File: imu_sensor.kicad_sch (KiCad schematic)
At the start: 10 parts, among them J2 JST_PH2.0_01x04, U1 LSM6DSL, U2 LIS2MDL

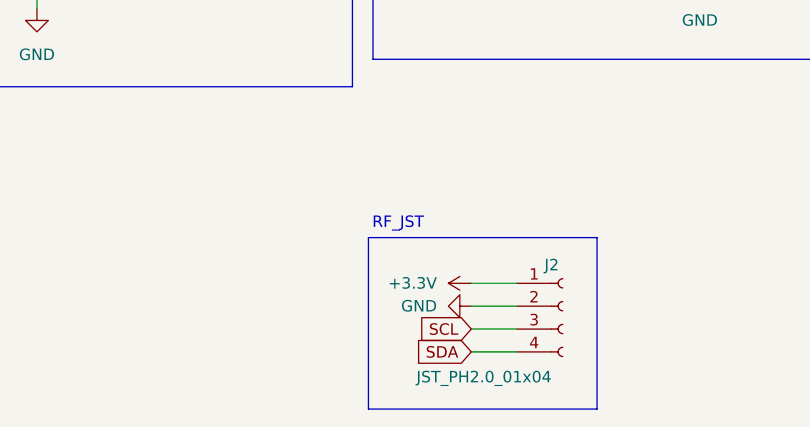
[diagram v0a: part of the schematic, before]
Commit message: Route Traces for ESP32 and related IO
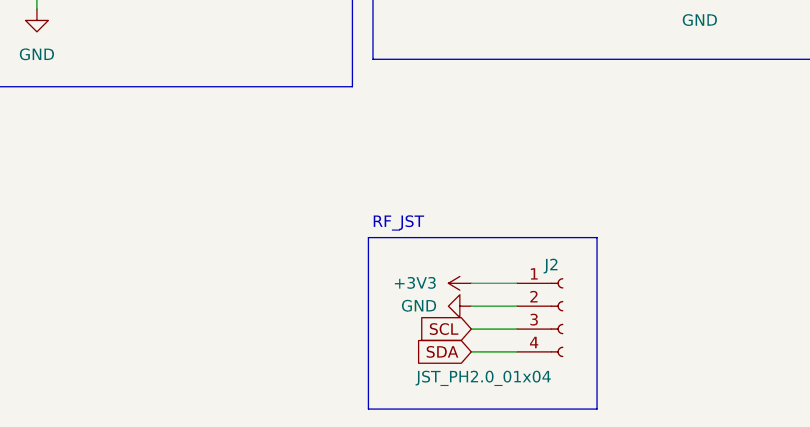
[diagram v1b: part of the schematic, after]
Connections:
- net +3.3V is gone; now on net +3V3: J2.1 (Pin_1)
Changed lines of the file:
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@@
 			)
 		)
-		(property "Value" "+3.3V"
+		(property "Value" "+3V3"
 			(at 118.11 121.9199 90)
 			(effects

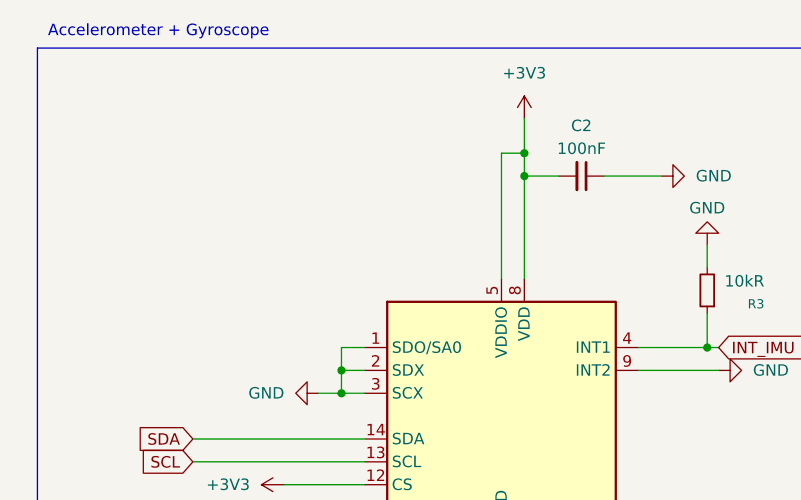
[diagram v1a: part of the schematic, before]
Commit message: Add Sensors and Silkscreen Adjustments
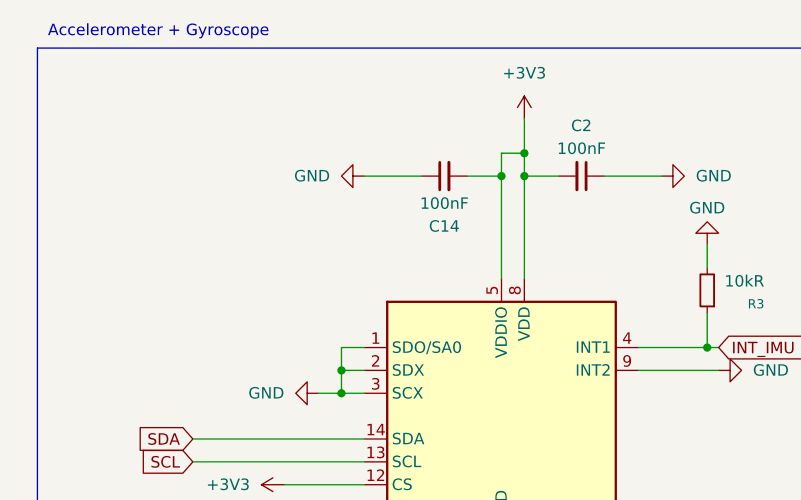
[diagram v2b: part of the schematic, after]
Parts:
- added C14: 100nF, Capacitor_SMD:C_0805_2012Metric_Pad1.18x1.45mm_HandSolder, symbol Device:C_Small
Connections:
- net +3V3: now also C14.2
- net GND: now also C14.1
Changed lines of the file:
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@@
+	)
+	(junction
+		(at 73.66 40.64)
+		(diameter 0)
+		(color 0 0 0 0)
 	)
 	(junction
@@
 	(wire
 		(pts
+			(xy 64.77 40.64) (xy 58.42 40.64)
+		)
+		(stroke
+			(width 0)
+			(type default)
+		)
+	)
+	(wire
+		(pts
 			(xy 172.72 59.69) (xy 172.72 62.23)
 		)
@@
 	(wire
 		(pts
+			(xy 69.85 40.64) (xy 73.66 40.64)
+		)
+		(stroke
+			(width 0)
+			(type default)
+		)
+	)
+	(wire
+		(pts
 			(xy 119.38 64.77) (xy 134.62 64.77)
 		)
@@
 	(wire
 		(pts
-			(xy 73.66 38.1) (xy 73.66 52.07)
+			(xy 73.66 38.1) (xy 73.66 40.64)
 		)
 		(stroke
@@
 		(pts
 			(xy 147.32 35.56) (xy 147.32 38.1)
+		)
+		(stroke
+			(width 0)
+			(type default)
+		)
+	)
+	(wire
+		(pts
+			(xy 73.66 40.64) (xy 73.66 52.07)
 		)
 		(stroke
@@
 	)
 	(symbol
+		(lib_id "Device:C_Small")
+		(at 67.31 40.64 90)
+		(mirror x)
+		(unit 1)
+		(exclude_from_sim no)
+		(in_bom yes)
+		(on_board yes)
+		(dnp no)
+		(property "Reference" "C14"
+			(at 67.31 46.228 90)
+			(effects
+				(font
+					(size 1.27 1.27)
+				)
+			)
+		)
+		(property "Value" "100nF"
+			(at 67.31 43.688 90)
+			(effects
+				(font
+					(size 1.27 1.27)
+				)
+			)
+		)
+		(property "Footprint" "Capacitor_SMD:C_0805_2012Metric_Pad1.18x1.45mm_HandSolder"
+			(at 67.31 40.64 0)
+			(effects
+				(font
+					(size 1.27 1.27)
+				)
+				(hide yes)
+			)
+		)
+		(property "Datasheet" "~"
+			(at 67.31 40.64 0)
+			(effects
+				(font
+					(size 1.27 1.27)
+				)
+				(hide yes)
+			)
+		)
+		(property "Description" "Unpolarized capacitor, small symbol"
+			(at 67.31 40.64 0)
+			(effects
+				(font
+					(size 1.27 1.27)
+				)
+				(hide yes)
+			)
+		)
+		(pin "2"
+		)
+		(pin "1"
+		)
+		(instances
+			(project "imu"
+				(path "/c0c3b276-ae23-48c2-9824-bf30dce5574d/819dc26d-f273-4edf-ac8c-4ee164d27f8f"
+					(reference "C14")
+					(unit 1)
+				)
+			)
+		)
+	)
+	(symbol
 		(lib_id "power:GND")
 		(at 53.34 64.77 270)
@@
 					(unit 1)
 				)
+			)
+		)
+	)
+	(symbol
+		(lib_id "power:GND")
+		(at 58.42 40.64 270)
+		(mirror x)
+		(unit 1)
+		(exclude_from_sim no)
+		(in_bom yes)
+		(on_board yes)
+		(dnp no)
+		(fields_autoplaced yes)
+		(property "Reference" "#PWR046"
+			(at 52.07 40.64 0)
+			(effects
+				(font
+					(size 1.27 1.27)
+				)
+				(hide yes)
+			)
+		)
+		(property "Value" "GND"
+			(at 54.61 40.6401 90)
+			(effects
+				(font
+					(size 1.27 1.27)
+				)
+				(justify right)
+			)
+		)
+		(property "Footprint" ""
+			(at 58.42 40.64 0)
+			(effects
+				(font
+					(size 1.27 1.27)
+				)
+				(hide yes)
+			)
+		)
+		(property "Datasheet" ""
+			(at 58.42 40.64 0)
+			(effects
+				(font
+					(size 1.27 1.27)
+				)
+				(hide yes)
+			)
+		)
+		(property "Description" "Power symbol creates a global label with name \"GND\" , ground"
+			(at 58.42 40.64 0)
+			(effects
+				(font
+					(size 1.27 1.27)
+				)
+				(hide yes)
+			)
+		)
+		(pin "1"
+		)
+		(instances
+			(project "imu"
+				(path "/c0c3b276-ae23-48c2-9824-bf30dce5574d/819dc26d-f273-4edf-ac8c-4ee164d27f8f"
+					(reference "#PWR046")
+					(unit 1)
+				)
